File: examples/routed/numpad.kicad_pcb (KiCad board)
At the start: 2 copper layers, 76.2 x 95.2 mm, 53 parts, among them J1 HRO-TYPE-C-31-M-12, SW0 SW_Cherry_MX_1.00u_PCB, SW1 SW_Cherry_MX_1.00u_PCB, SW10 SW_Cherry_MX_1.00u_PCB, SW11 SW_Cherry_MX_1.00u_PCB, SW12 SW_Cherry_MX_1.00u_PCB, SW13 SW_Cherry_MX_1.00u_PCB, SW14 SW_Cherry_MX_1.00u_PCB, SW15 SW_Cherry_MX_1.00u_PCB, SW16 SW_Cherry_MX_1.00u_PCB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

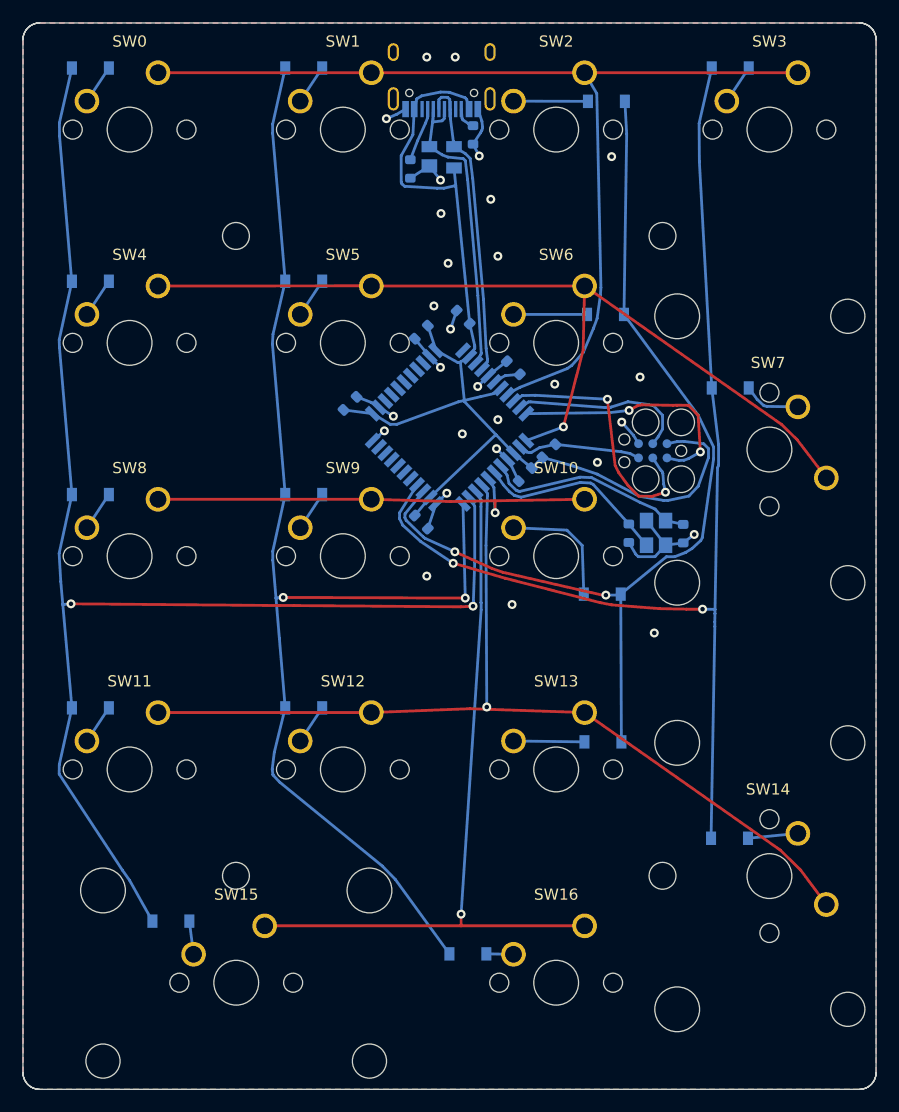
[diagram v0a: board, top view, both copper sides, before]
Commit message: Add numpad as ordered
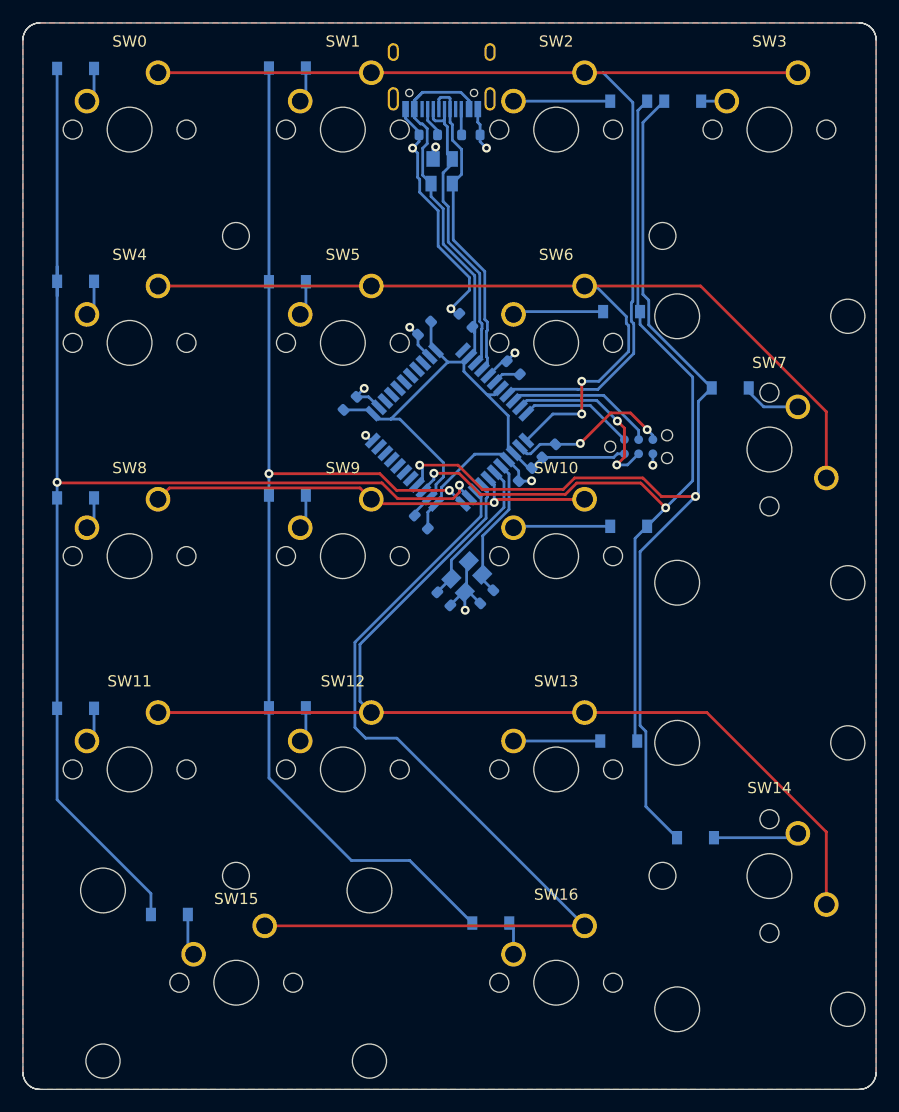
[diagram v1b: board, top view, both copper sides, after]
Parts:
- Jx1: value Tag-Connect_TC2030-IDC-FP_2x03_P1.27mm_Vertical -> Tag-Connect_TC2030-IDC-NL_2x03_P1.27mm_Vertical; footprint Tag-Connect_TC2030-IDC-FP_2x03_P1.27mm_Vertical -> Tag-Connect_TC2030-IDC-NL_2x03_P1.27mm_Vertical
- moved C3 18.4 mm to (57.4, 67.3), turned to -135 degrees
- moved C2 17.5 mm to (53.6, 67.4), turned to -45 degrees
- moved X1 17.3 mm to (55.6, 65.5), turned to 45 degrees
- moved D11 6.50 mm to (70.1, 61.0)
- moved D4 5.18 mm to (74.9, 23.0)
- moved R1 3.44 mm to (52.2, 26.0), turned to 0 degrees
- moved D17 3.43 mm to (57.8, 96.4)
- moved D15 3.04 mm to (76.1, 88.8)
- moved D3 1.99 mm to (70.1, 23.0)
- moved D7 1.46 mm to (69.5, 41.8)
- moved D10 1.45 mm to (39.6, 58.2)
- moved D6 1.45 mm to (39.6, 39.1)
- moved D13 1.45 mm to (39.6, 77.2)
- moved D2 1.45 mm to (39.6, 20.0)
- moved D14 1.41 mm to (69.2, 80.1)
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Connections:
- R2 pad 1: GND -> usb-cc2
- R2 pad 2: usb-cc2 -> GND
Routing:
- net GND: track 43.6 -> 62.4 mm, vias 28 -> 11
- net usb-vcc: track 102.3 -> 86.8 mm
- net matrix-4: track 67.6 -> 82.4 mm, vias 1 -> 0
- net icsp-miso: track 22.3 -> 10.3 mm, vias 2 -> 0
- net matrix-1: track 82.2 -> 92.5 mm, vias 1 -> 2
- net icsp-sck: track 23.8 -> 13.5 mm, vias 2 -> 0
- net matrix-3: track 86.0 -> 96.3 mm, vias 1 -> 0
- net matrix-0: track 90.6 -> 98.0 mm
- net xtal2: track 18.9 -> 12.8 mm
- net matrix-6: track 111.7 -> 105.8 mm
- net matrix-5: track 125.8 -> 120.8 mm
- net xtal1: track 17.2 -> 13.3 mm
- net icsp-reset: track 11.0 -> 14.8 mm, vias 0 -> 2
- net switch-diode-14: track 4.48 -> 7.65 mm
- net switch-diode-10: track 11.1 -> 8.69 mm
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- removed copper zone on B.Cu, net GND
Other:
- board text added: "kbtb/numpad mk1 peterklein.dev"
- board text removed: "maude (a number pad) peterklein.dev"
